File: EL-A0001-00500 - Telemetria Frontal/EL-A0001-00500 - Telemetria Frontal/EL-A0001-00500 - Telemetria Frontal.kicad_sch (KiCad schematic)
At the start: 3 parts, among them J1 1-776087-1, U1 YAAJ_BluePill, U2 MP1584

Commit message: Telemetria frontal
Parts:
- added C1, C2: C, Capacitor_SMD:C_0805_2012Metric, symbol Device:C
- added D1: 1N4007, Diode_THT:D_DO-41_SOD81_P10.16mm_Horizontal, symbol Diode:1N4007
- added D2: LED, LED_THT:LED_D5.0mm, symbol Device:LED
- added J2: Conn_01x02_Male, Connector_PinHeader_2.54mm:PinHeader_1x02_P2.54mm_Vertical, symbol Connector:Conn_01x02_Male
- added J3, J4, J6: Conn_01x04_Male, Connector_PinHeader_2.54mm:PinHeader_1x04_P2.54mm_Vertical, symbol Connector:Conn_01x04_Male
- added J5: UART, Connector_PinHeader_2.54mm:PinHeader_1x03_P2.54mm_Vertical, symbol Connector:Conn_01x03_Male
- added R1: 220, Resistor_SMD:R_0805_2012Metric, symbol Device:R_US
- added R10, R12, R14, R16, R18, R2, R20, R22, R24, R4, R6, R8: 10k, Resistor_SMD:R_0805_2012Metric, symbol Device:R_US
- added R11, R13, R15, R17, R19, R21, R23, R25, R3, R5, R7, R9: 20k, Resistor_SMD:R_0805_2012Metric, symbol Device:R_US
- added U3, U4: LM324, Package_DIP:DIP-14_W7.62mm_LongPads, symbol Amplifier_Operational:LM324
- added U5: TJA1050-Module, Cheetah:TJA1050-Module, symbol Cheetah:TJA1050-Module
- U1: footprint STM32 Blue Pill:YAAJ_BluePill_1 -> STM32:YAAJ_BluePill_1
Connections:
- net at U1.1 (PB12): now also J6.1 (Pin_1)
- net at U1.12 (PB4): now also J4.1 (Pin_1)
- net at U1.13 (PB5): now also J4.2 (Pin_2)
- net at U1.14 (PB6): now also J4.3 (Pin_3)
- net at U1.15 (PB7): now also J4.4 (Pin_4)
- net at U1.16 (PB8): now also U5.3 (RX)
- net at U1.17 (PB9): now also U5.2 (TX)
- net +5V: now reaches U1.18 (5V)
- net +5V: now also U2.OUT1+ (VOUT+), U2.OUT2+ (VOUT+), D2.2 (A), U5.1 (VCC)
- net GNDREF: now reaches U1.19 (GND)
- net GNDREF: now also U1.39 (GND), U1.40 (GND), U2.IN1 (VIN-), U2.IN2 (VIN-), U2.OUT1 (VOUT-), U2.OUT2 (VOUT-), C1.2, C2.2, J2.2 (Pin_2), J3.1 (Pin_1), J3.2 (Pin_2), J3.3 (Pin_3), J3.4 (Pin_4), J5.1 (Pin_1), R1.2, R11.1, R13.1, R15.1, R17.1, R19.1, R21.1, R23.1, R25.1, R3.1, R5.1, R7.1, R9.1, U3.11 (V-), U4.11 (V-), U5.4 (GND)
- net at U1.2 (PB13): now also J6.2 (Pin_2)
- net at U1.25 (PA0): now also U4.1, U4.2 (-)
- net at U1.26 (PA1): now also U4.6 (-), U4.7
- net at U1.27 (PA2): now also U4.8, U4.9 (-)
- net at U1.28 (PA3): now also U4.13 (-), U4.14
- net at U1.29 (PA4): now also U3.1, U3.2 (-)
- net at U1.3 (PB14): now also J6.3 (Pin_3)
- net at U1.30 (PA5): now also U3.6 (-), U3.7
- net at U1.31 (PA6): now also U3.8, U3.9 (-)
- net at U1.32 (PA7): now also U3.13 (-), U3.14
- net at U1.33 (PB0): now also R2.1, R3.2
- net at U1.34 (PB1): now also R4.1, R5.2
- net at U1.35 (PB10): now also R10.1, R11.2
- net at U1.36 (PB11): now also R16.1, R17.2
- net at U1.4 (PB15): now also J6.4 (Pin_4)
- net at U1.6 (PA9): now also J5.2 (Pin_2)
- net at U1.7 (PA10): now also J5.3 (Pin_3)
- net at U2.IN1+ (VIN+), U2.IN2+ (VIN+): now also C1.1, C2.1, D1.1 (K), U3.4 (V+), U4.4 (V+)
- new net: R12.1, R13.2, U3.10 (+)
- new net: R14.1, R15.2, U4.10 (+)
- new net: R22.1, R23.2, U3.3 (+)
- new net: R6.1, R7.2, U3.12 (+)
- new net: R24.1, R25.2, U4.3 (+)
- new net: D2.1 (K), R1.1
- new net: R8.1, R9.2, U4.12 (+)
- new net: R18.1, R19.2, U3.5 (+)
- new net: R20.1, R21.2, U4.5 (+)
- new net: D1.2 (A), J2.1 (Pin_1)
- new net ADC_1: R12.2
- new net ADC_2: R6.2
- new net DI_1: R2.2
- new net DI_2: R4.2
- new net DI_3: R10.2
- new net DI_4: R16.2
- new net ENCODER: R18.2
- new net PRESSURE_1: R14.2
- new net PRESSURE_2: R8.2
- new net PRESSURE_3: R22.2
- new net TPS_1: R24.2
- new net TPS_2: R20.2
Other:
- moved on the sheet: J1, U1

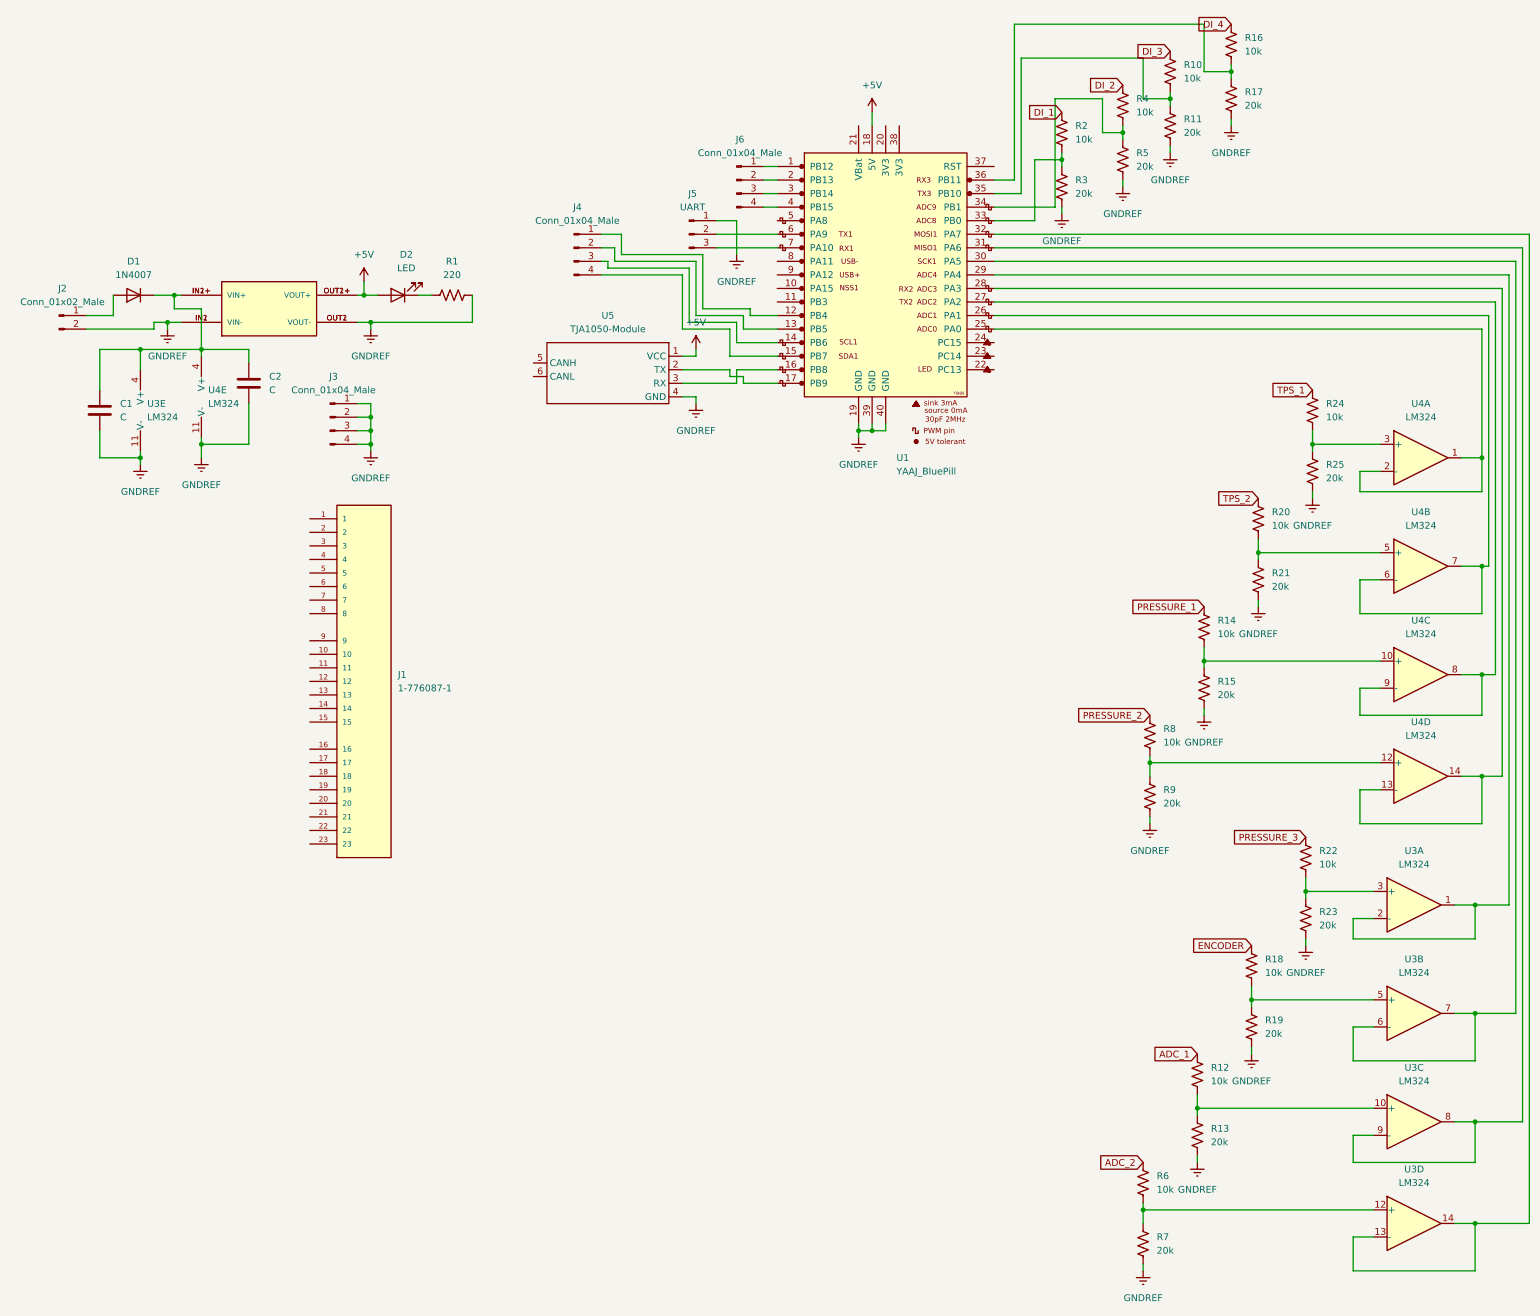
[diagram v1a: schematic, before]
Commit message: ADD: fusiveis BMS
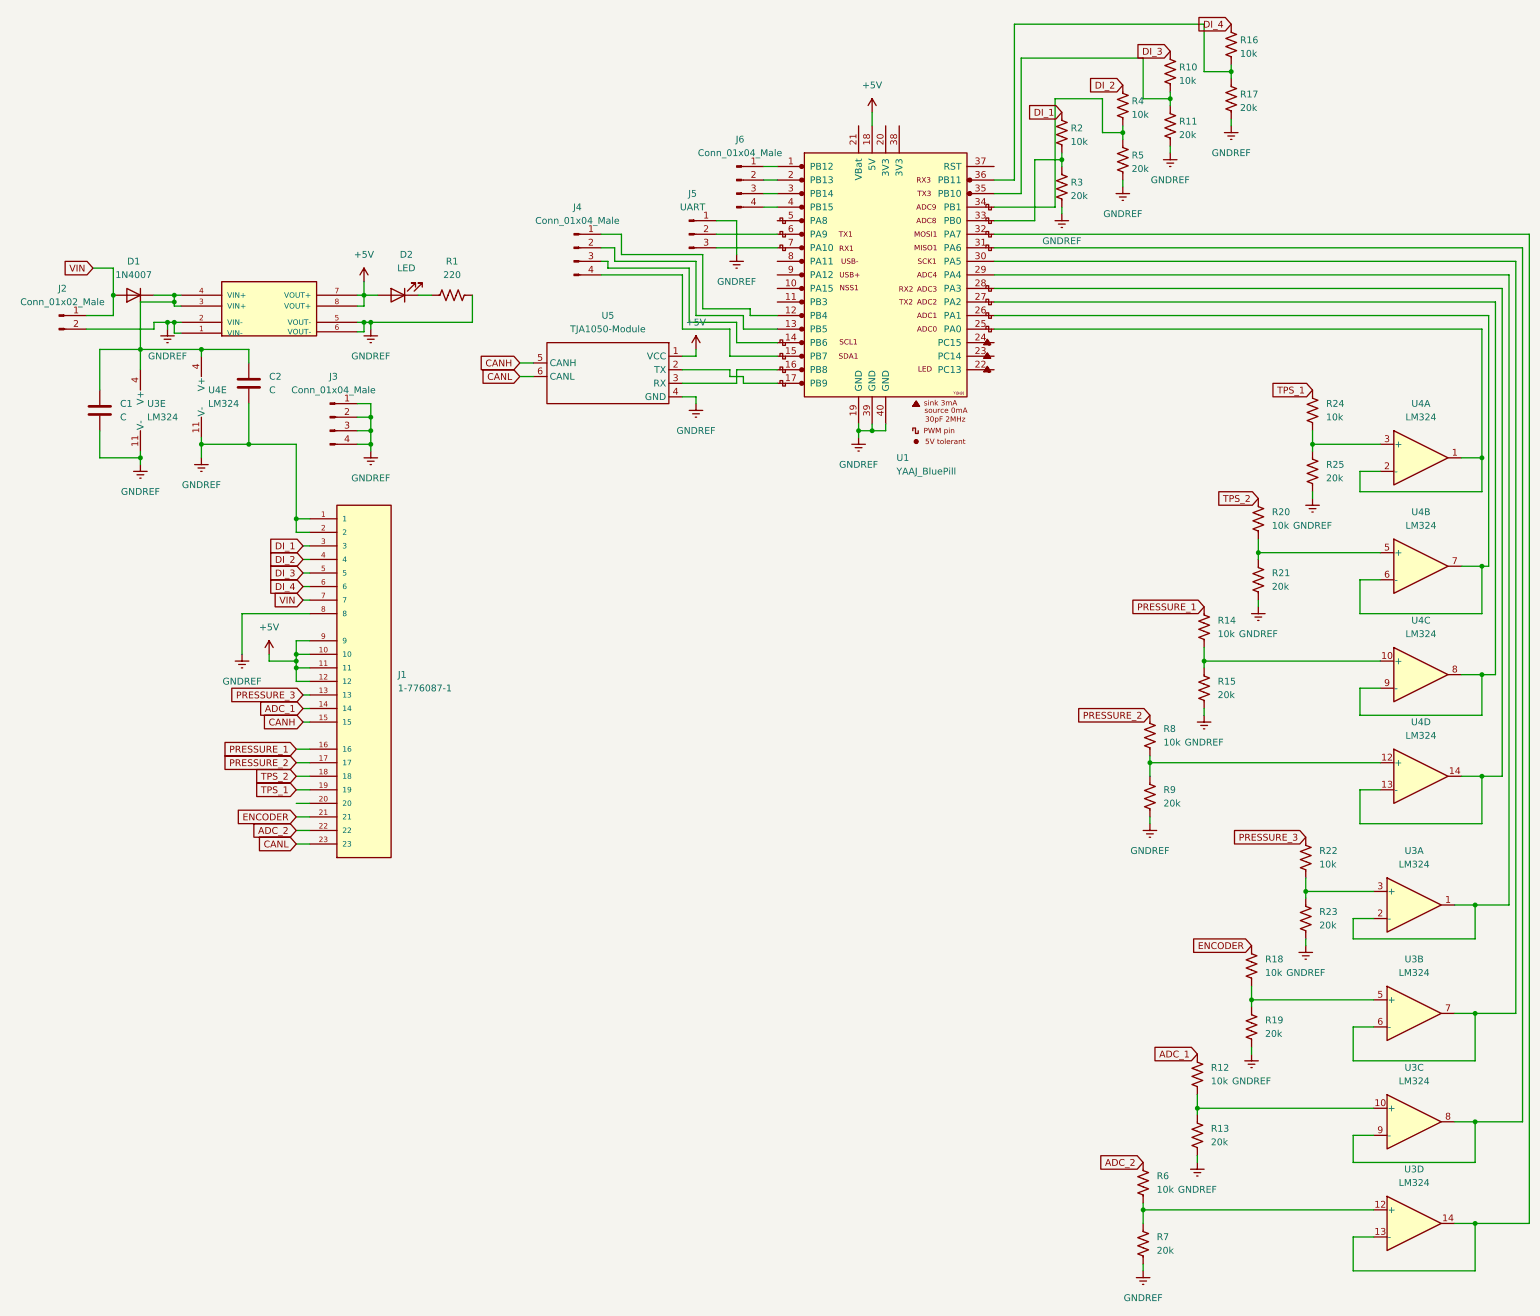
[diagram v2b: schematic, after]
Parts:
- R10, R11, R16, R17, R2, R3, R4, R5: footprint Resistor_SMD:R_0805_2012Metric -> Resistor_THT:R_Axial_DIN0207_L6.3mm_D2.5mm_P10.16mm_Horizontal
- U2: footprint MP1584:DC-BRICK -> Cheetah:DC-BRICK
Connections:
- net +5V: now also J1.10, J1.11, J1.12, J1.9, U2.7 (VOUT+), U2.8 (VOUT+); no longer U2.OUT1+ (VOUT+), U2.OUT2+ (VOUT+)
- net ADC_1: now also J1.14
- net ADC_2: now also J1.22
- net DI_1: now also J1.3
- net DI_2: now also J1.4
- net DI_3: now also J1.5
- net DI_4: now also J1.6
- net ENCODER: now also J1.21
- net GNDREF: now also J1.1, J1.2, J1.8, U2.1 (VIN-), U2.2 (VIN-), U2.5 (VOUT-), U2.6 (VOUT-); no longer U2.IN1 (VIN-), U2.IN2 (VIN-), U2.OUT1 (VOUT-), U2.OUT2 (VOUT-)
- net PRESSURE_1: now also J1.16
- net PRESSURE_2: now also J1.17
- net PRESSURE_3: now also J1.13
- net TPS_1: now also J1.19
- net TPS_2: now also J1.18
- net at C1.1, C2.1, D1.1 (K)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: now also U2.3 (VIN+), U2.4 (VIN+); no longer U2.IN1+ (VIN+), U2.IN2+ (VIN+)
- net CANH: now reaches U5.5 (CANH)
- net CANH: now also J1.15
- net CANL: now reaches U5.6 (CANL)
- net CANL: now also J1.23
- net VIN: now reaches J1.7
- net VIN: now also D1.2 (A), J2.1 (Pin_1)
